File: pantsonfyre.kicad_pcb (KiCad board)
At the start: 2 copper layers, 24 parts, among them J1 3.5mm TRRS, J2 USB_C_Receptacle, SW1 SW_Push, SW2 SW_Push, SW3 SW_Push, U1 CAP1206-x-SL, U2 STM32C011J4Mx, U3 MCP4725xxx-xCH, U4 CAP1206-x-SL, U5 CAP1206-x-SL, U7 AMS1117-3.3

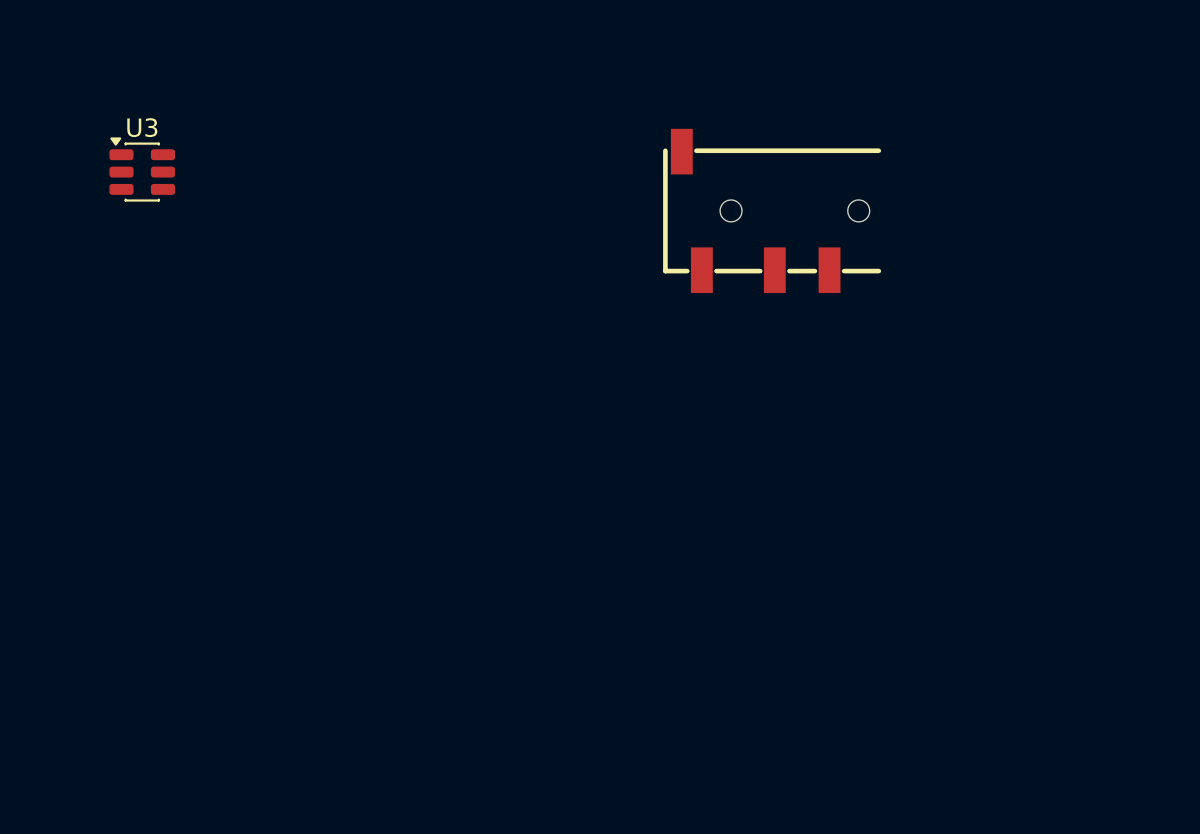
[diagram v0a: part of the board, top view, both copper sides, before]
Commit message: Add d-class amp + fixes
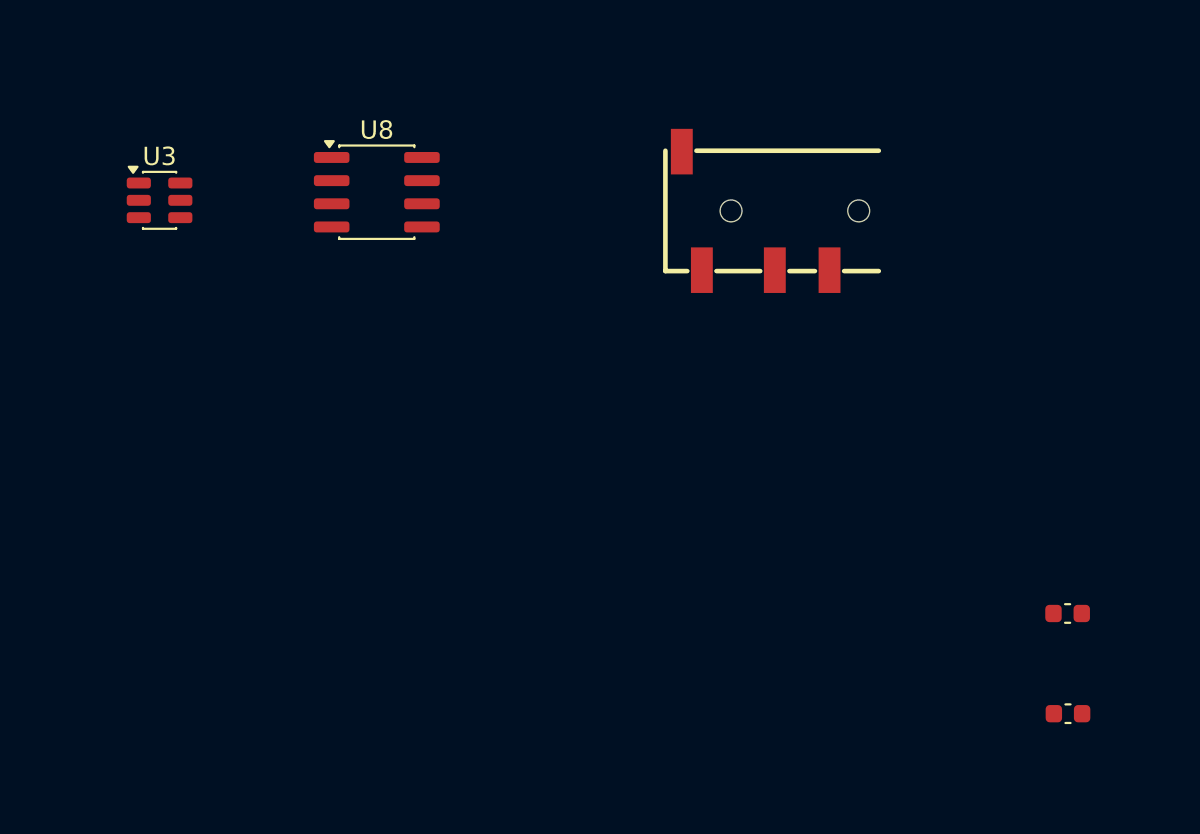
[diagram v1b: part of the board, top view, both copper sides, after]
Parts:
- added C5: 10uF, PCM_SparkFun-Capacitor:C_0603_1608Metric, F.Cu at (260.3, 129.9)
- added C6: 0.1uF, PCM_SparkFun-Capacitor:C_0603_1608Metric, F.Cu at (260.3, 135.3)
- added U8: PAM8302AAD, Package_SO:SOIC-8_3.9x4.9mm_P1.27mm, F.Cu at (222.4, 106.8)
- moved U3 1.82 mm to (210.5, 107.2)
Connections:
- net Net-(U7-VI) renamed 5V
- J1 pad R2: GND -> Net-(U8-OUT-)
- J1 pad S: GND -> Net-(U8-OUT-)
- U3 pad 1: unconnected-(U3-VOUT-Pad1) -> Net-(U3-VOUT)

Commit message: Did lots of stuff + removed the custom footprint for header
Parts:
- added C10: 0.1uF, PCM_SparkFun-Capacitor:C_0603_1608Metric, F.Cu at (136.7, 51.0)
- added C11: 0.1uF, PCM_SparkFun-Capacitor:C_0603_1608Metric, F.Cu at (166.9, 49.4)
- added C12: 1.0uF, PCM_SparkFun-Capacitor:C_0603_1608Metric, F.Cu at (166.9, 51.0)
- added C13: 0.1uF, PCM_SparkFun-Capacitor:C_0603_1608Metric, F.Cu at (197.1, 51.0)
- added C14: 1.0uF, PCM_SparkFun-Capacitor:C_0603_1608Metric, F.Cu at (197.1, 49.4)
- added C7: 10uF, PCM_SparkFun-Capacitor:C_0603_1608Metric, F.Cu at (170.4, 37.0)
- added C8: 1.0uF, PCM_SparkFun-Capacitor:C_0603_1608Metric, F.Cu at (172.1, 37.0)
- added C9: 1.0uF, PCM_SparkFun-Capacitor:C_0603_1608Metric, F.Cu at (136.7, 49.3)
- added R6: 10k, PCM_SparkFun-Resistor:R_0603_1608Metric, F.Cu at (174.4, 37.0)
- C6: value 0.1uF -> 1.0uF
- U6: footprint Slider:STLink-Headers -> Connector_PinHeader_2.54mm:PinHeader_1x04_P2.54mm_Vertical
- U7: footprint Package_TO_SOT_SMD:TO-263-5_TabPin3 -> Package_TO_SOT_SMD:SOT-223-3_TabPin2
- moved U5 130.5 mm to (191.1, 54.9)
- moved C6 121.7 mm to (186.1, 38.8), turned to 90 degrees
- moved UTouch3 120.0 mm to (177.7, 109.9)
- moved C5 118.4 mm to (184.5, 38.8), turned to 90 degrees
- moved SW3 115.1 mm to (177.7, 64.0)
- moved U4 114.6 mm to (160.9, 54.8)
- moved UTouch2 105.9 mm to (147.6, 109.9)
- moved U1 104.5 mm to (130.7, 54.8)
- moved SW2 100.4 mm to (147.5, 64.0)
- moved UTouch1 96.2 mm to (117.4, 109.9)
- moved SW1 90.1 mm to (117.4, 64.0)
- moved J1 85.5 mm to (194.8, 38.8)
- moved U8 80.1 mm to (179.7, 38.9)
- moved U3 76.3 mm to (173.0, 40.7), turned to -90 degrees
- moved U2 72.5 mm to (153.4, 39.8)
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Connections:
- net 5V renamed /+5V
- U8 pad 1: unconnected-(U8-~{SD}-Pad1) -> Net-(U8-~{SD})
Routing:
- net 3.3V: track 0.00 -> 260.7 mm, vias 0 -> 8
- net Net-(U1-SMCLK): track 0.00 -> 143.8 mm
- net Net-(U1-SMDATA): track 0.00 -> 128.2 mm, vias 0 -> 2
- net Net-(U5-CS1): track 0.00 -> 93.0 mm
- net Net-(U1-CS1): track 0.00 -> 93.0 mm
- net Net-(U4-CS1): track 0.00 -> 93.0 mm
- net Net-(U5-CS2): track 0.00 -> 72.4 mm
- net Net-(U4-CS2): track 0.00 -> 72.4 mm
- net Net-(U1-CS2): track 0.00 -> 72.0 mm
- net Net-(U4-CS3): track 0.00 -> 57.6 mm
- net Net-(U2-PA10/PA12): track 0.00 -> 53.9 mm, vias 0 -> 2
- net Net-(U5-CS3): track 0.00 -> 53.3 mm
- net Net-(U1-CS3): track 0.00 -> 53.3 mm
- net Net-(U2-PA0/PA1/PA2/PF2): track 0.00 -> 45.8 mm, vias 0 -> 2
- net Net-(U5-CS4): track 0.00 -> 42.9 mm
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- added copper zone on B.Cu, net GND
- added copper zone on F.Cu, net GND
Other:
- board outline added: 100.9 x 121.4 mm

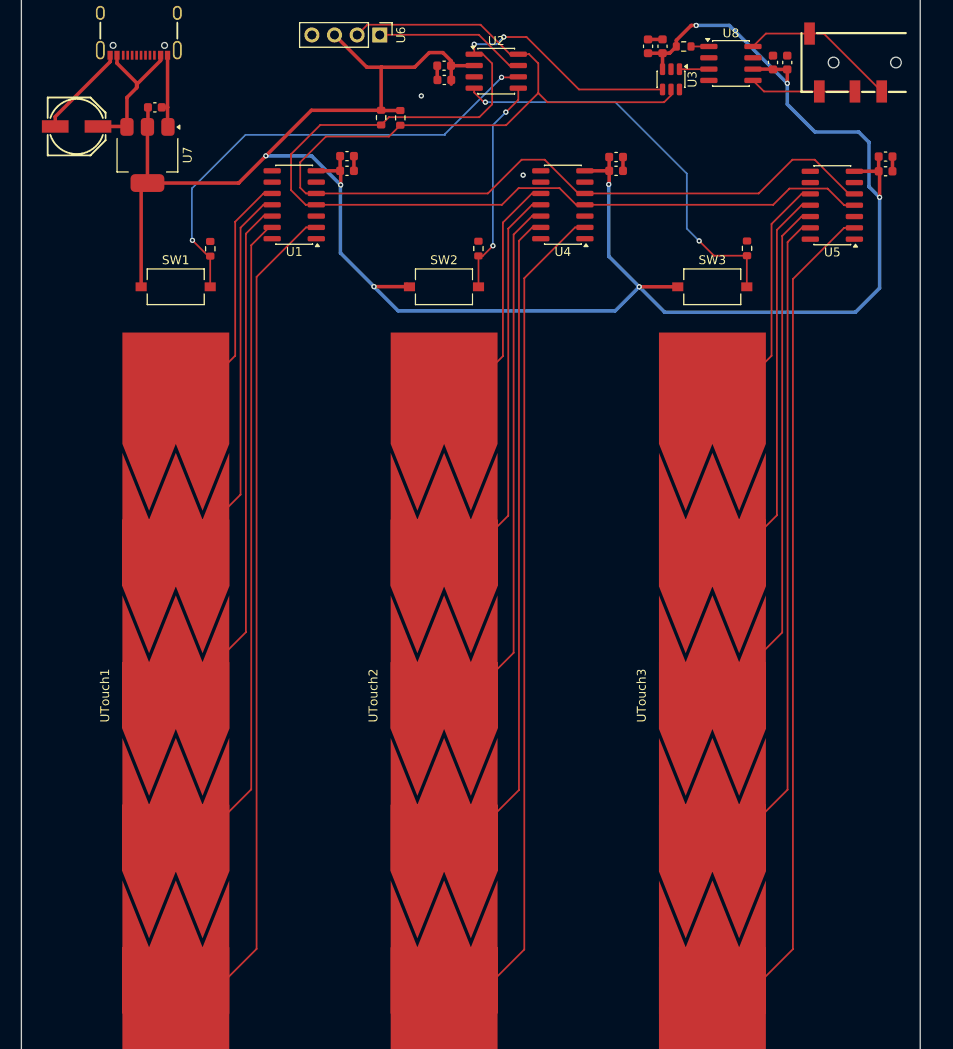
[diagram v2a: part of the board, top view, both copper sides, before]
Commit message: Add resistor to gnd for ALERT pin because erc was yelling at me
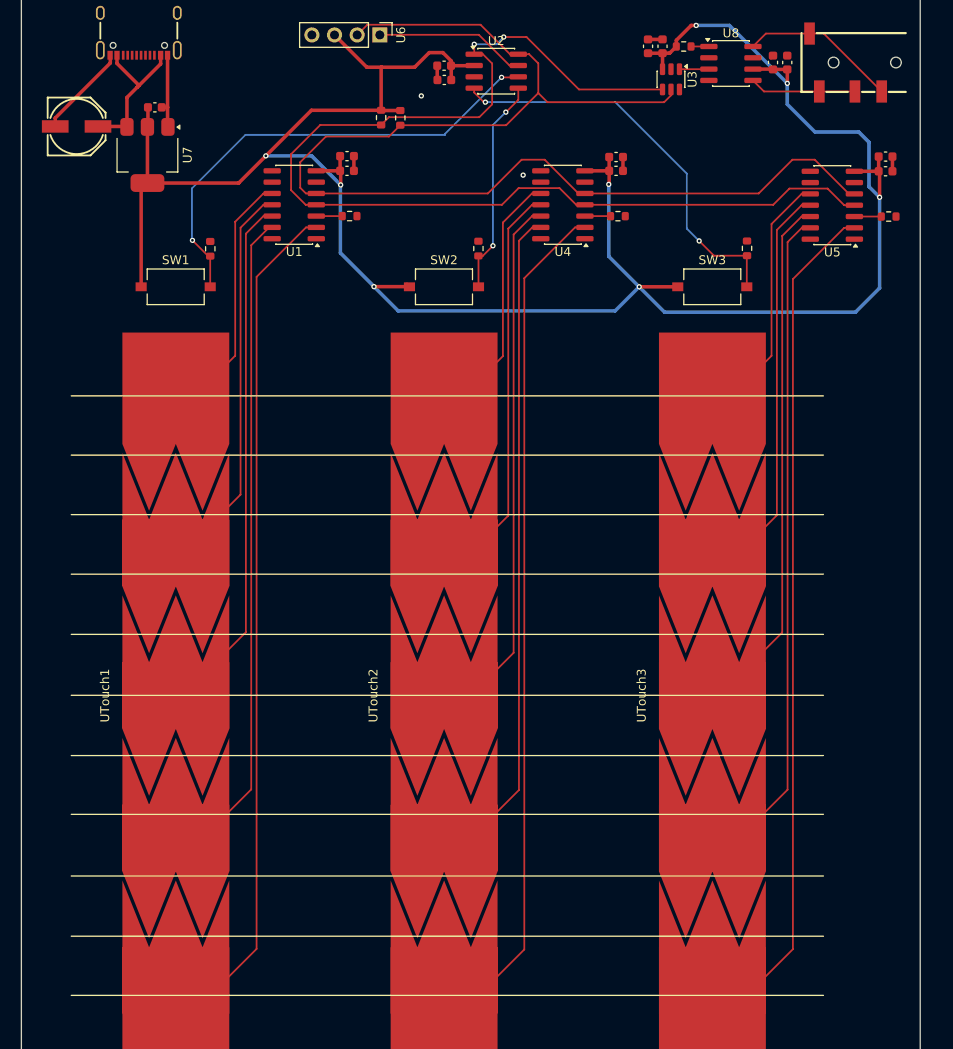
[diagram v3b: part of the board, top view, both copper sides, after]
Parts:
- added R7: 1k, PCM_SparkFun-Resistor:R_0603_1608Metric, F.Cu at (136.9, 56.1)
- added R8: 1k, PCM_SparkFun-Resistor:R_0603_1608Metric, F.Cu at (167.1, 56.1)
- added R9: 1k, PCM_SparkFun-Resistor:R_0603_1608Metric, F.Cu at (197.4, 56.1)
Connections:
- U1 pad 3: GND -> Net-(U1-ALERT#)
- U4 pad 3: GND -> Net-(U4-ALERT#)
- U5 pad 3: GND -> Net-(U5-ALERT#)
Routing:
- net Net-(U5-ALERT#): track 0.00 -> 3.02 mm
- net Net-(U1-ALERT#): track 0.00 -> 2.92 mm
- net Net-(U4-ALERT#): track 0.00 -> 2.89 mm

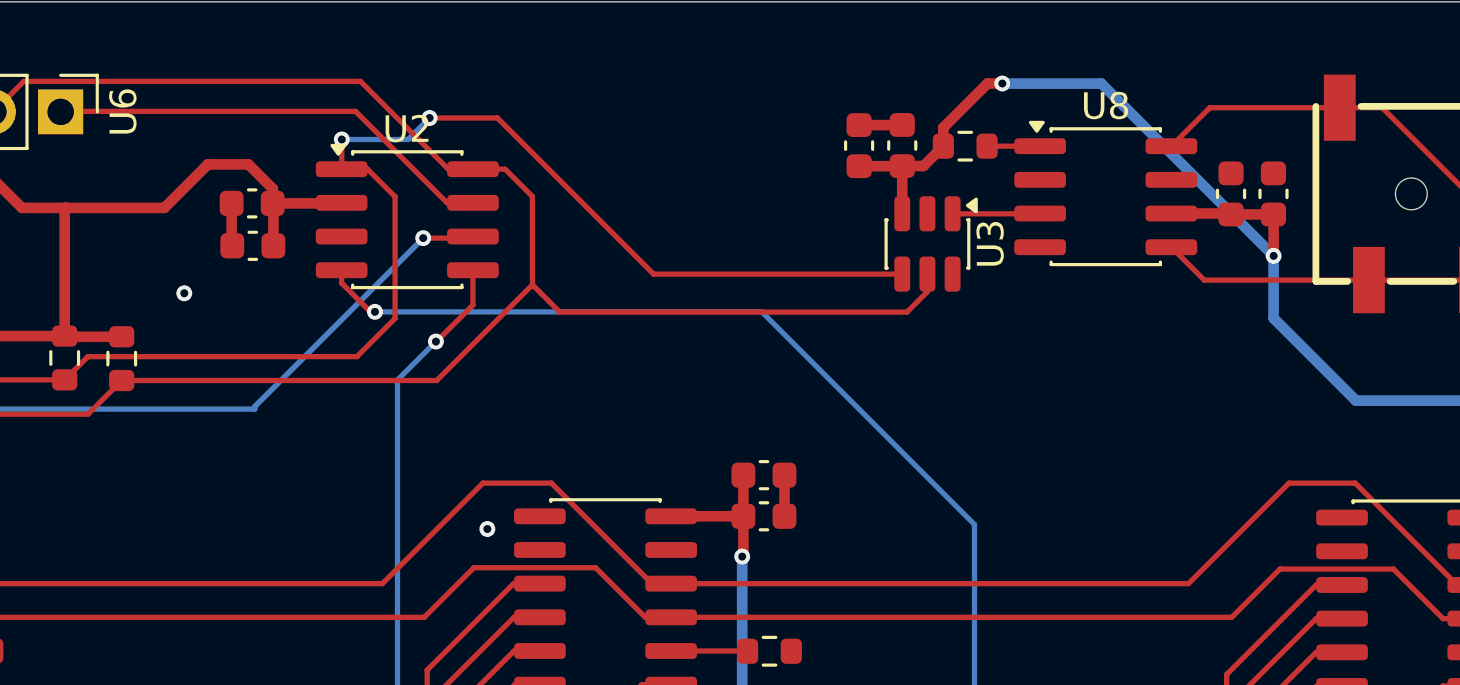
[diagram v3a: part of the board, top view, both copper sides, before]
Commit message: Fix missing connections to gnd pour
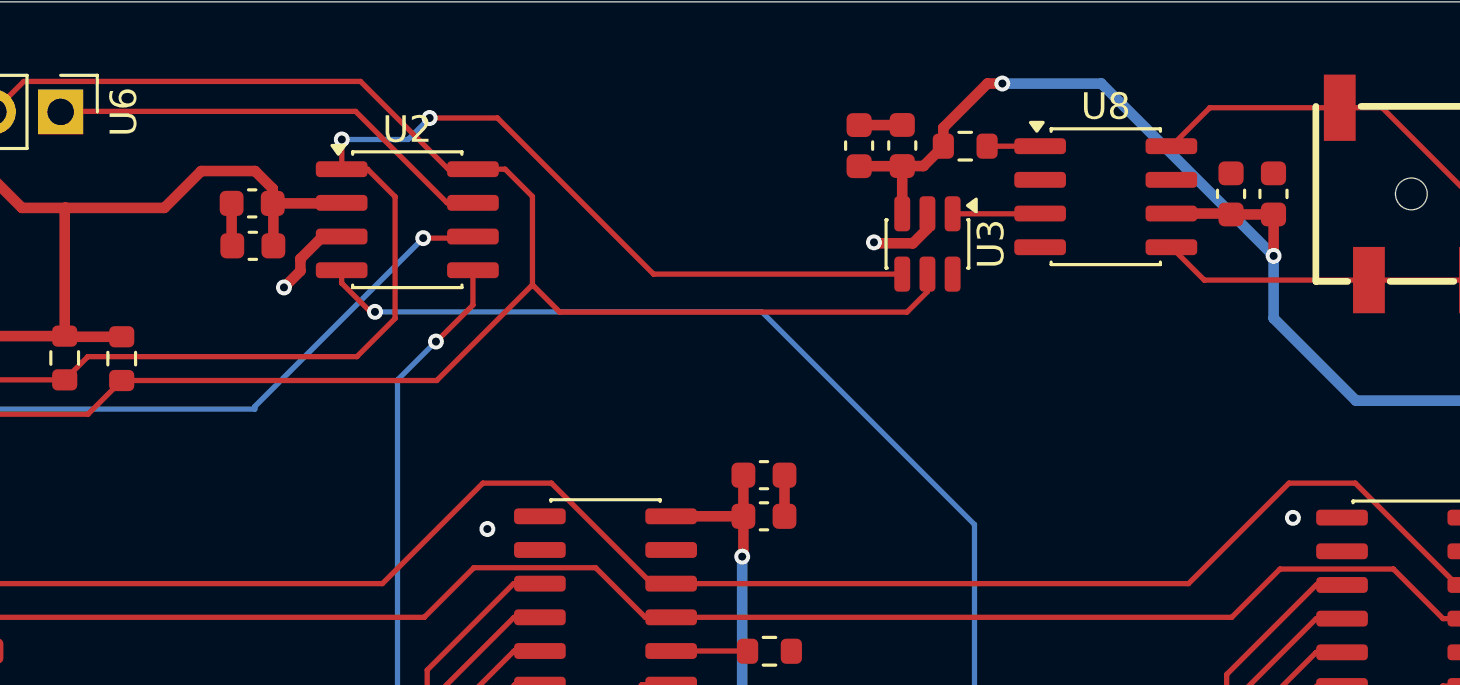
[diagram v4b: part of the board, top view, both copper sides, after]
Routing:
- net GND: track 27.7 -> 33.8 mm, vias 2 -> 4
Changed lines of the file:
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@@
+	)
+	(segment
+		(start 150.92625 40.44)
+		(end 150.21 40.44)
+		(width 0.4)
+		(layer "F.Cu")
+		(net "GND")
 	)
 	(segment
@@
 	)
 	(segment
+		(start 173.01625 39.5825)
+		(end 173.01625 40.147684)
+		(width 0.4)
+		(layer "F.Cu")
+		(net "GND")
+	)
+	(segment
 		(start 116.50825 38.015)
 		(end 116.50825 43.865)
@@
 	)
 	(segment
+		(start 173.01625 40.147684)
+		(end 172.468934 40.695)
+		(width 0.4)
+		(layer "F.Cu")
+		(net "GND")
+	)
+	(segment
 		(start 110.05825 38.015)
 		(end 110.08325 38.04)
@@
 	)
 	(segment
+		(start 149.37 41.28)
+		(end 149.37 41.74)
+		(width 0.4)
+		(layer "F.Cu")
+		(net "GND")
+	)
+	(segment
 		(start 197.87625 49.39)
 		(end 197.87625 51.04)
@@
 	)
 	(segment
+		(start 172.468934 40.695)
+		(end 171.035 40.695)
+		(width 0.4)
+		(layer "F.Cu")
+		(net "GND")
+	)
+	(segment
 		(start 110.08325 38.04)
 		(end 110.08325 38.88675)
@@
 	)
 	(segment
+		(start 171.035 40.695)
+		(end 171 40.66)
+		(width 0.4)
+		(layer "F.Cu")
+		(net "GND")
+	)
+	(segment
+		(start 149.37 41.74)
+		(end 148.75 42.36)
+		(width 0.4)
+		(layer "F.Cu")
+		(net "GND")
+	)
+	(segment
+		(start 150.21 40.44)
+		(end 149.37 41.28)
+		(width 0.4)
+		(layer "F.Cu")
+		(net "GND")
+	)
+	(segment
 		(start 137.42625 49.34)
 		(end 137.42625 50.99)
@@
 	)
 	(via
-		(at 144.99125 42.58)
+		(at 148.75 42.36)
 		(size 0.6)
 		(drill 0.3)
@@
 		(net "GND")
 	)
+	(via
+		(at 186.8 51.05)
+		(size 0.6)
+		(drill 0.3)
+		(layers "F.Cu" "B.Cu")
+		(free yes)
+		(net "GND")
+	)
+	(via
+		(at 171 40.66)
+		(size 0.6)
+		(drill 0.3)
+		(layers "F.Cu" "B.Cu")
+		(free yes)
+		(net "GND")
+	)
 	(segment
 		(start 175.28125 34.67)
@@
 	)
 	(segment
+		(start 144.24125 39.36)
+		(end 140.53125 39.36)
+		(width 0.4)
+		(layer "F.Cu")
+		(net "3.3V")
+	)
+	(segment
 		(start 132.65625 44.195)
 		(end 127.54125 49.31)
@@
 	)
 	(segment
-		(start 147.41125 37.72)
-		(end 145.88125 37.72)
-		(width 0.4)
-		(layer "F.Cu")
-		(net "3.3V")
-	)
-	(segment
 		(start 135.94125 51.055)
 		(end 135.87625 50.99)
@@
 	)
 	(segment
+		(start 145.63125 37.97)
+		(end 144.24125 39.36)
+		(width 0.4)
+		(layer "F.Cu")
+		(net "3.3V")
+	)
+	(segment
 		(start 193.60125 51.04)
 		(end 196.32625 51.04)
@@
 	)
 	(segment
-		(start 148.32625 38.635)
-		(end 147.41125 37.72)
-		(width 0.4)
-		(layer "F.Cu")
-		(net "3.3V")
-	)
-	(segment
 		(start 143.37125 63.717371)
 		(end 143.66101 64.007131)
@@
 	)
 	(segment
+		(start 138.87 39.36)
+		(end 140.53125 39.36)
+		(width 0.4)
+		(layer "F.Cu")
+		(net "3.3V")
+	)
+	(segment
+		(start 170.44125 37.7875)
+		(end 172.06125 37.7875)
+		(width 0.4)
+		(layer "F.Cu")
+		(net "3.3V")
+	)
+	(segment
+		(start 172.06625 37.7825)
+		(end 172.86625 37.7825)
+		(width 0.4)
+		(layer "F.Cu")
+		(net "3.3V")
+	)
+	(segment
+		(start 142.63125 44.22)
+		(end 140.50625 44.22)
+		(width 0.4)
+		(layer "F.Cu")
+		(net "3.3V")
+	)
+	(segment
+		(start 186.07125 39.6125)
+		(end 186.06625 39.6075)
+		(width 0.4)
+		(layer "F.Cu")
+		(net "3.3V")
+	)
+	(segment
 		(start 148.32625 39.19)
 		(end 148.32625 38.635)
@@
 	)
 	(segment
-		(start 138.87 39.36)
-		(end 140.53125 39.36)
-		(width 0.4)
-		(layer "F.Cu")
-		(net "3.3V")
-	)
-	(segment
-		(start 145.88125 37.72)
-		(end 144.24125 39.36)
-		(width 0.4)
-		(layer "F.Cu")
-		(net "3.3V")
-	)
-	(segment
-		(start 170.44125 37.7875)
-		(end 172.06125 37.7875)
-		(width 0.4)
-		(layer "F.Cu")
-		(net "3.3V")
-	)
-	(segment
-		(start 172.06625 37.7825)
-		(end 172.86625 37.7825)
-		(width 0.4)
-		(layer "F.Cu")
-		(net "3.3V")
-	)
-	(segment
-		(start 142.63125 44.22)
-		(end 140.50625 44.22)
-		(width 0.4)
-		(layer "F.Cu")
-		(net "3.3V")
-	)
-	(segment
-		(start 186.07125 39.6125)
-		(end 186.06625 39.6075)
-		(width 0.4)
-		(layer "F.Cu")
-		(net "3.3V")
-	)
-	(segment
-		(start 144.24125 39.36)
-		(end 140.53125 39.36)
-		(width 0.4)
-		(layer "F.Cu")
-		(net "3.3V")
-	)
-	(segment
 		(start 166.07625 49.44)
 		(end 166.07625 50.99)
@@
 	)
 	(segment
+		(start 148.32625 38.635)
+		(end 147.66125 37.97)
+		(width 0.4)
+		(layer "F.Cu")
+		(net "3.3V")
+	)
+	(segment
 		(start 114.25125 46.06)
 		(end 114.25125 52.36)
 		(width 0.4)
 		(layer "F.Cu")
+		(net "3.3V")
+	)
+	(segment
+		(start 147.66125 37.97)
+		(end 145.63125 37.97)
+		(width 0.4)
+		(layer "F.Cu")
